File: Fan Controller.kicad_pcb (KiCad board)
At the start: 4 copper layers, 33 x 96 mm, 37 parts, among them J1 Power Input, J2 4-Pin Fan Header, J3 4-Pin Fan Header, J4 I2C, J5 Conn_01x04, J6 Conn_01x06, J7 Conn_01x05, Q1 SQD19P06-60L_GE3, U1 ESP32-C3-SuperMini, U2 AP63205QWU-7, U3 SN74LVC2G06DBVR

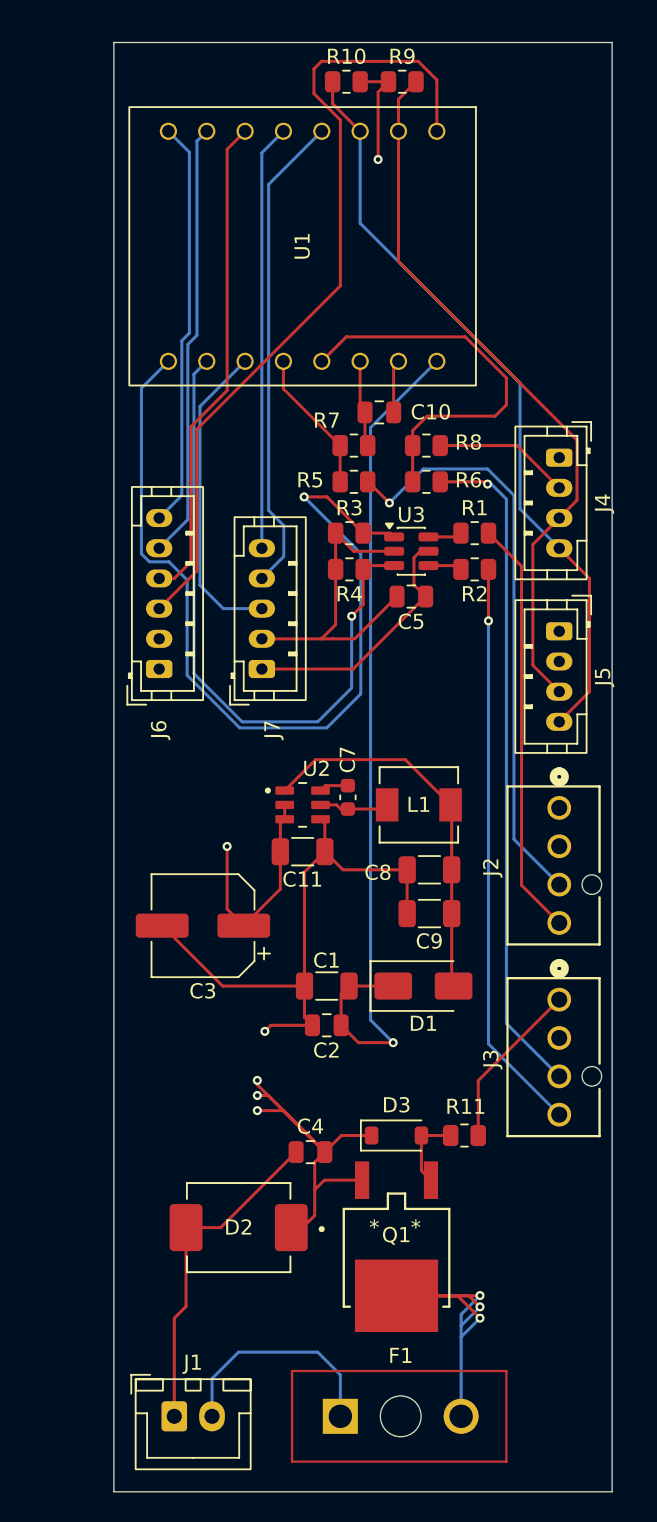
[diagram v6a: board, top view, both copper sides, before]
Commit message: Schematic optimisations
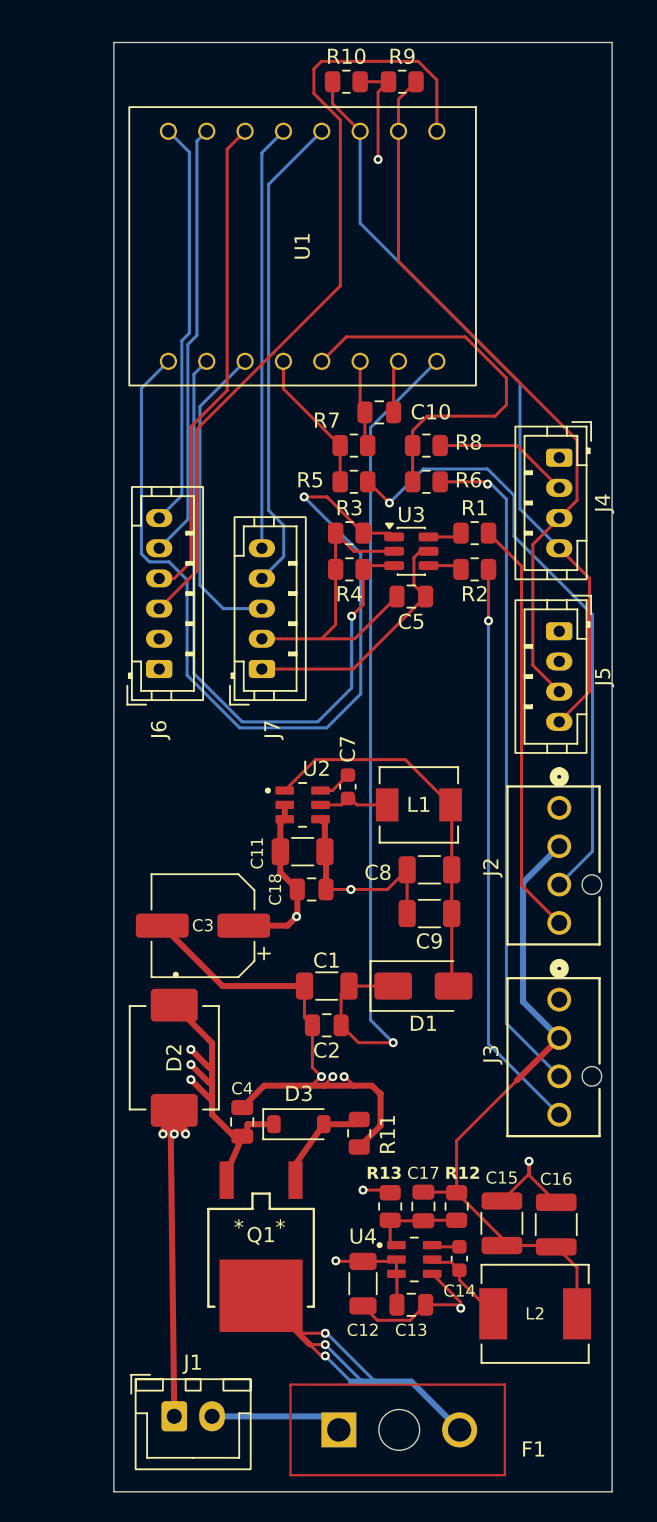
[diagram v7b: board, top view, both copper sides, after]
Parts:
- added C12: 10µF, Capacitor_SMD:C_1206_3216Metric, F.Cu at (168.0, 119.7)
- added C13: 100nF, Capacitor_SMD:C_0805_2012Metric, F.Cu at (171.2, 121.1)
- added C14: 100nF, Capacitor_SMD:C_0603_1608Metric, F.Cu at (174.4, 118.0)
- added C15: 22µF / 25V, Capacitor_SMD:C_1210_3225Metric, F.Cu at (177.2, 115.7)
- added C16: 22µF / 25V, Capacitor_SMD:C_1210_3225Metric, F.Cu at (180.8, 115.8)
- added C17: 56pF C0G, Capacitor_SMD:C_0805_2012Metric, F.Cu at (172.0, 114.6)
- added C18: 100nF, Capacitor_SMD:C_0805_2012Metric, F.Cu at (164.6, 93.6)
- added L2: 15µH, custom_footprints:IND_SPM6530T-150M-HZ, F.Cu at (179.4, 121.7)
- added R12: 422k, Resistor_SMD:R_0805_2012Metric, F.Cu at (174.2, 114.6)
- added R13: 30.1k, Resistor_SMD:R_0805_2012Metric, F.Cu at (169.8, 114.6)
- added U4: AP63201QWU-7, custom_footprints:SOT95P280X100-6N, F.Cu at (171.4, 118.1)
- J5: value Conn_01x04 -> I2C
- J6: value Conn_01x06 -> Expansion 1
- J7: value Conn_01x05 -> Expansion 2
- moved D2 12.0 mm to (155.5, 104.8), turned to -90 degrees
- moved Q1 8.97 mm to (161.2, 118.0)
- moved R11 6.97 mm to (167.8, 109.8), turned to 90 degrees
- moved D3 6.51 mm to (163.8, 109.2)
- moved C4 4.94 mm to (160.0, 109.0), turned to 90 degrees
- moved F1 0.91 mm to (170.4, 129.4)
- moved C7 0.70 mm to (167.0, 86.8)
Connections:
- J2 pad 2: /+12V_PROTECTED -> /+12V_FAN
- J3 pad 2: /+12V_PROTECTED -> /+12V_FAN
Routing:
- net /+12V_FAN: track 0.00 -> 43.8 mm
- net GND: track 97.3 -> 118.4 mm, vias 1 -> 10
- net /+12V: track 15.1 -> 8.50 mm
- net /FAN_BUCK_FB: track 0.00 -> 6.36 mm
- net /12V_RAW_FUSED: track 29.6 -> 35.8 mm
- net /FAN_BUCK_SW: track 0.00 -> 6.03 mm
- net /+12V_PROTECTED: track 46.6 -> 41.2 mm, vias 4 -> 5
- net /FAN_BUCK_BST: track 0.00 -> 2.03 mm
- net Net-(J2-Pin_3): track 38.9 -> 40.8 mm
- net Net-(D3-A): track 5.15 -> 5.95 mm
- net Net-(U2-SW): track 4.64 -> 5.16 mm

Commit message: Better placement of R11
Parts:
- moved R11 5.50 mm to (163.1, 106.8), turned to 0 degrees
- moved L2 1.81 mm to (179.2, 119.9)
- moved C12 1.81 mm to (167.8, 117.9)
- moved C15 1.81 mm to (177.0, 113.9)
- moved C16 1.81 mm to (180.6, 114.0)
- moved R13 1.81 mm to (169.6, 112.8)
- moved U4 1.81 mm to (171.2, 116.3)
- moved C13 1.81 mm to (171.0, 119.3)
- moved C14 1.81 mm to (174.2, 116.2)
- moved C17 1.81 mm to (171.8, 112.8)
- moved R12 1.81 mm to (174.0, 112.8)
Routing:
- net GND: track 118.4 -> 107.5 mm, vias 10 -> 11
- net /+12V_FAN: track 43.8 -> 45.0 mm
